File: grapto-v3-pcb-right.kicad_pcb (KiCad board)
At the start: 2 copper layers, 134.1 x 25.9 mm, 2 parts

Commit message: Switch positions.
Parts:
- added D10: D, Diode_SMD:D_SOD-323_HandSoldering, F.Cu at (114.3, 326.6)
- added D11: D, Diode_SMD:D_SOD-323_HandSoldering, F.Cu at (109.2, 329.5)
- added D12: D, Diode_SMD:D_SOD-323_HandSoldering, F.Cu at (119.3, 323.6)
- added D13: D, Diode_SMD:D_SOD-323_HandSoldering, F.Cu at (104.2, 329.5)
- added D14: D, Diode_SMD:D_SOD-323_HandSoldering, F.Cu at (99.2, 329.5)
- added D15: D, Diode_SMD:D_SOD-323_HandSoldering, F.Cu at (109.2, 326.6)
- added D16: D, Diode_SMD:D_SOD-323_HandSoldering, F.Cu at (84.0, 323.6)
- added D17: D, Diode_SMD:D_SOD-323_HandSoldering, F.Cu at (134.5, 323.6)
- added D18: D, Diode_SMD:D_SOD-323_HandSoldering, F.Cu at (89.0, 323.6)
- added D19: D, Diode_SMD:D_SOD-323_HandSoldering, F.Cu at (84.0, 326.6)
- added D20: D, Diode_SMD:D_SOD-323_HandSoldering, F.Cu at (89.0, 326.6)
- added D21: D, Diode_SMD:D_SOD-323_HandSoldering, F.Cu at (94.1, 323.6)
- added D22: D, Diode_SMD:D_SOD-323_HandSoldering, F.Cu at (99.2, 323.6)
- added D23: D, Diode_SMD:D_SOD-323_HandSoldering, F.Cu at (94.1, 326.6)
- added D24: D, Diode_SMD:D_SOD-323_HandSoldering, F.Cu at (89.0, 329.5)
- added D25: D, Diode_SMD:D_SOD-323_HandSoldering, F.Cu at (104.2, 323.6)
- added D26: D, Diode_SMD:D_SOD-323_HandSoldering, F.Cu at (94.1, 329.5)
- added D27: D, Diode_SMD:D_SOD-323_HandSoldering, F.Cu at (99.2, 326.6)
- added D28: D, Diode_SMD:D_SOD-323_HandSoldering, F.Cu at (104.2, 326.6)
- added D29: D, Diode_SMD:D_SOD-323_HandSoldering, F.Cu at (109.2, 323.6)
- added D3: D, Diode_SMD:D_SOD-323_HandSoldering, F.Cu at (119.3, 329.5)
- added D30: D, Diode_SMD:D_SOD-323_HandSoldering, F.Cu at (114.3, 323.6)
- added D4: D, Diode_SMD:D_SOD-323_HandSoldering, F.Cu at (114.3, 329.5)
- added D5: D, Diode_SMD:D_SOD-323_HandSoldering, F.Cu at (124.4, 326.6)
- added D6: D, Diode_SMD:D_SOD-323_HandSoldering, F.Cu at (129.4, 323.6)
- added D7: D, Diode_SMD:D_SOD-323_HandSoldering, F.Cu at (84.0, 329.5)
- added D8: D, Diode_SMD:D_SOD-323_HandSoldering, F.Cu at (124.4, 323.6)
- added D9: D, Diode_SMD:D_SOD-323_HandSoldering, F.Cu at (119.3, 326.6)
- added J1: USB_C_Receptacle, grapto-v3-pcb-right:Connector_GCT_USB4500, F.Cu at (234.4, 268.5)
- added J2: USB_C_Receptacle, grapto-v3-pcb-right:Connector_GCT_USB4500, F.Cu at (220.2, 268.5)
- added SW1: SW_Push, kaihl_choc:SW_Kailh_Choc_V1, F.Cu at (100.0, 43.0)
- added SW10: SW_Push, kaihl_choc:SW_Kailh_Choc_V1, F.Cu at (157.0, 56.0)
- added SW11: SW_Push, kaihl_choc:SW_Kailh_Choc_V1, F.Cu at (176.0, 75.0)
- added SW12: SW_Push, kaihl_choc:SW_Kailh_Choc_V1, F.Cu at (195.0, 94.0)
- added SW13: SW_Push, kaihl_choc:SW_Kailh_Choc_V1, F.Cu at (100.0, 81.0)
- added SW14: SW_Push, kaihl_choc:SW_Kailh_Choc_V1, F.Cu at (119.0, 75.0)
- added SW15: SW_Push, kaihl_choc:SW_Kailh_Choc_V1, F.Cu at (138.0, 70.0)
- added SW16: SW_Push, kaihl_choc:SW_Kailh_Choc_V1, F.Cu at (157.0, 75.0)
- added SW17: SW_Push, kaihl_choc:SW_Kailh_Choc_V1, F.Cu at (176.0, 94.0)
- added SW18: SW_Push, kaihl_choc:SW_Kailh_Choc_V1, F.Cu at (195.0, 113.0)
- added SW19: SW_Push, kaihl_choc:SW_Kailh_Choc_V1, F.Cu at (100.0, 100.0)
- added SW2: SW_Push, kaihl_choc:SW_Kailh_Choc_V1, F.Cu at (119.0, 37.0)
- added SW20: SW_Push, kaihl_choc:SW_Kailh_Choc_V1, F.Cu at (119.0, 94.0)
- added SW21: SW_Push, kaihl_choc:SW_Kailh_Choc_V1, F.Cu at (138.0, 89.0)
- added SW22: SW_Push, kaihl_choc:SW_Kailh_Choc_V1, F.Cu at (157.0, 94.0)
- added SW23: SW_Push, kaihl_choc:SW_Kailh_Choc_V1, F.Cu at (176.0, 113.0)
- added SW24: SW_Push, kaihl_choc:SW_Kailh_Choc_V1, F.Cu at (195.0, 147.0)
- added SW25: SW_Push, kaihl_choc:SW_Kailh_Choc_V1, F.Cu at (62.4, 143.7)
- added SW26: SW_Push, kaihl_choc:SW_Kailh_Choc_V1, F.Cu at (119.0, 113.0)
- added SW27: SW_Push, kaihl_choc:SW_Kailh_Choc_V1, F.Cu at (138.0, 108.0)
- added SW28: SW_Push, kaihl_choc:SW_Kailh_Choc_V1, F.Cu at (157.0, 113.0)
- added SW29: SW_Push, kaihl_choc:SW_Kailh_Choc_V1, F.Cu at (99.0, 120.8)
- added SW3: SW_Push, kaihl_choc:SW_Kailh_Choc_V1, F.Cu at (138.0, 32.0)
- added SW30: SW_Push, kaihl_choc:SW_Kailh_Choc_V1, F.Cu at (78.6, 128.9)
- added SW4: SW_Push, kaihl_choc:SW_Kailh_Choc_V1, F.Cu at (157.0, 37.0)
- added SW5: SW_Push, kaihl_choc:SW_Kailh_Choc_V1, F.Cu at (176.0, 56.0)
- added SW6: SW_Push, kaihl_choc:SW_Kailh_Choc_V1, F.Cu at (195.0, 75.0)
- added SW7: SW_Push, kaihl_choc:SW_Kailh_Choc_V1, F.Cu at (100.0, 62.0)
- added SW8: SW_Push, kaihl_choc:SW_Kailh_Choc_V1, F.Cu at (119.0, 56.0)
- added SW9: SW_Push, kaihl_choc:SW_Kailh_Choc_V1, F.Cu at (138.0, 51.0)
- D1, D2: value LED -> D; footprint LED_THT:LED_D3.0mm -> Diode_SMD:D_SOD-323_HandSoldering
- moved D1 223.2 mm to (124.4, 329.5)
- moved D2 220.6 mm to (129.4, 326.6)
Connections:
- D1 pad 2: Net-(D1-Pad2) -> col0
- D2 pad 2: Net-(D2-Pad2) -> col1
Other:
- board size 134.1 x 25.9 mm -> 147.1 x 190.9 mm

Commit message: updated sw pos
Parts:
- J1, J2: moved to B.Cu
- moved J2 221.6 mm to (63.9, 111.5)
- moved J1 220.3 mm to (79.7, 111.5)
- moved SW10 2.00 mm to (157.0, 58.0)
- moved SW11 2.00 mm to (176.0, 77.0)
- moved SW12 2.00 mm to (195.0, 96.0)
- moved SW14 2.00 mm to (119.0, 77.0)
- moved SW15 2.00 mm to (138.0, 72.0)
- moved SW16 2.00 mm to (157.0, 77.0)
- moved SW17 2.00 mm to (176.0, 96.0)
- moved SW18 2.00 mm to (195.0, 115.0)
- moved SW2 2.00 mm to (119.0, 39.0)
- moved SW20 2.00 mm to (119.0, 96.0)
- moved SW21 2.00 mm to (138.0, 91.0)
- moved SW22 2.00 mm to (157.0, 96.0)
- moved SW23 2.00 mm to (176.0, 115.0)
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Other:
- board size 147.1 x 190.9 mm -> 48.3 x 22.9 mm

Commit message: Edge cuts
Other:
- board size 48.3 x 22.9 mm -> 150.2 x 129.8 mm
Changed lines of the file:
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@@
     )
   )
-  (gr_line (start 176.145 131.77) (end 127.885 131.77) (layer Edge.Cuts) (width 0.05))
-  (gr_line (start 171.065 154.63) (end 176.145 131.77) (layer Edge.Cuts) (width 0.05))
-  (gr_line (start 132.965 154.63) (end 171.065 154.63) (layer Edge.Cuts) (width 0.05))
-  (gr_line (start 127.885 131.77) (end 132.965 154.63) (layer Edge.Cuts) (width 0.05))
+  (gr_line (start 88.430 113.140) (end 88.430 114.640) (angle 90) (layer Edge.Cuts) (width 0.05))
+  (gr_line (start 88.430 114.640) (end 94.630 114.640) (angle 90) (layer Edge.Cuts) (width 0.05))
+  (gr_arc (start 94.630 110.940) (end 94.630 114.640) (angle -180.000) (layer Edge.Cuts) (width 0.05))
+  (gr_line (start 94.630 107.240) (end 92.830 107.240) (angle 90) (layer Edge.Cuts) (width 0.05))
+  (gr_line (start 92.830 107.240) (end 92.830 35.037) (angle 90) (layer Edge.Cuts) (width 0.05))
+  (gr_arc (start 93.330 35.037) (end 93.225 34.549) (angle -77.903) (layer Edge.Cuts) (width 0.05))
+  (gr_line (start 93.225 34.549) (end 103.932 32.254) (angle 90) (layer Edge.Cuts) (width 0.05))
+  (gr_arc (start 104.037 32.743) (end 104.537 32.743) (angle -102.097) (layer Edge.Cuts) (width 0.05))
+  (gr_line (start 104.537 32.743) (end 104.537 32.763) (angle 90) (layer Edge.Cuts) (width 0.05))
+  (gr_arc (start 108.237 32.763) (end 104.537 32.763) (angle -180.000) (layer Edge.Cuts) (width 0.05))
+  (gr_line (start 112.332 30.454) (end 131.524 26.340) (angle 90) (layer Edge.Cuts) (width 0.05))
+  (gr_arc (start 131.629 26.829) (end 131.629 26.329) (angle -12.097) (layer Edge.Cuts) (width 0.05))
+  (gr_line (start 131.629 26.329) (end 144.276 26.329) (angle 90) (layer Edge.Cuts) (width 0.05))
+  (gr_arc (start 144.276 26.829) (end 144.403 26.346) (angle -14.737) (layer Edge.Cuts) (width 0.05))
+  (gr_line (start 144.403 26.346) (end 163.798 31.447) (angle 90) (layer Edge.Cuts) (width 0.05))
+  (gr_arc (start 163.671 31.931) (end 164.007 31.561) (angle -27.500) (layer Edge.Cuts) (width 0.05))
+  (gr_line (start 164.007 31.561) (end 192.921 57.813) (angle 90) (layer Edge.Cuts) (width 0.05))
+  (gr_line (start 202.178 67.427) (end 202.178 155.674) (angle 90) (layer Edge.Cuts) (width 0.05))
+  (gr_arc (start 201.678 155.674) (end 201.678 156.174) (angle -90.000) (layer Edge.Cuts) (width 0.05))
+  (gr_line (start 201.678 156.174) (end 186.978 156.174) (angle 90) (layer Edge.Cuts) (width 0.05))
+  (gr_line (start 63.846 153.805) (end 52.166 144.879) (angle 90) (layer Edge.Cuts) (width 0.05))
+  (gr_arc (start 52.470 144.482) (end 51.970 144.482) (angle -52.610) (layer Edge.Cuts) (width 0.05))
+  (gr_line (start 51.970 144.482) (end 51.970 113.140) (angle 90) (layer Edge.Cuts) (width 0.05))
+  (gr_line (start 51.970 113.140) (end 57.005 113.140) (angle 90) (layer Edge.Cuts) (width 0.05))
+  (gr_arc (start 112.437 30.942) (end 112.332 30.454) (angle -77.903) (layer Edge.Cuts) (width 0.05))
+  (gr_line (start 111.937 30.942) (end 111.937 32.763) (angle 90) (layer Edge.Cuts) (width 0.05))
+  (gr_arc (start 193.678 63.227) (end 190.939 60.740) (angle -132.237) (layer Edge.Cuts) (width 0.05))
+  (gr_arc (start 192.585 58.183) (end 192.956 58.519) (angle -90.000) (layer Edge.Cuts) (width 0.05))
+  (gr_line (start 192.956 58.519) (end 190.939 60.740) (angle 90) (layer Edge.Cuts) (width 0.05))
+  (gr_line (start 193.678 66.927) (end 201.678 66.927) (angle 90) (layer Edge.Cuts) (width 0.05))
+  (gr_arc (start 201.678 67.427) (end 202.178 67.427) (angle -90.000) (layer Edge.Cuts) (width 0.05))
+  (gr_arc (start 182.778 154.374) (end 186.478 154.374) (angle -180.000) (layer Edge.Cuts) (width 0.05))
+  (gr_line (start 186.478 154.374) (end 186.478 155.674) (angle 90) (layer Edge.Cuts) (width 0.05))
+  (gr_line (start 179.078 154.374) (end 179.078 155.674) (angle 90) (layer Edge.Cuts) (width 0.05))
+  (gr_line (start 178.578 156.174) (end 73.279 156.174) (angle 90) (layer Edge.Cuts) (width 0.05))
+  (gr_arc (start 186.978 155.674) (end 186.478 155.674) (angle -90.000) (layer Edge.Cuts) (width 0.05))
+  (gr_arc (start 178.578 155.674) (end 178.578 156.174) (angle -90.000) (layer Edge.Cuts) (width 0.05))
+  (gr_arc (start 69.079 153.874) (end 72.779 153.874) (angle -142.610) (layer Edge.Cuts) (width 0.05))
+  (gr_line (start 66.140 151.627) (end 64.547 153.712) (angle 90) (layer Edge.Cuts) (width 0.05))
+  (gr_line (start 72.779 153.874) (end 72.779 155.674) (angle 90) (layer Edge.Cuts) (width 0.05))
+  (gr_arc (start 64.149 153.408) (end 63.846 153.805) (angle -90.000) (layer Edge.Cuts) (width 0.05))
+  (gr_arc (start 73.279 155.674) (end 72.779 155.674) (angle -90.000) (layer Edge.Cuts) (width 0.05))
+  (gr_line (start 75.005 113.140) (end 75.005 119.340) (angle 90) (layer Edge.Cuts) (width 0.05))
+  (gr_line (start 75.005 119.340) (end 84.245 119.340) (angle 90) (layer Edge.Cuts) (width 0.05))
+  (gr_line (start 84.245 119.340) (end 84.245 113.140) (angle 90) (layer Edge.Cuts) (width 0.05))
+  (gr_line (start 66.245 113.140) (end 66.245 119.340) (angle 90) (layer Edge.Cuts) (width 0.05))
+  (gr_line (start 66.245 119.340) (end 57.005 119.340) (angle 90) (layer Edge.Cuts) (width 0.05))
+  (gr_line (start 57.005 119.340) (end 57.005 113.140) (angle 90) (layer Edge.Cuts) (width 0.05))
+  (gr_line (start 66.245 113.140) (end 75.005 113.140) (angle 90) (layer Edge.Cuts) (width 0.05))
+  (gr_line (start 84.245 113.140) (end 88.430 113.140) (angle 90) (layer Edge.Cuts) (width 0.05))
 )

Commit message: Fix usb connectors
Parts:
- J1, J2: value USB_C_Receptacle -> USB_C_Receptacle_USB2.0
- moved J1 18.2 mm to (61.6, 113.1)
- moved J2 15.8 mm to (79.6, 113.1)

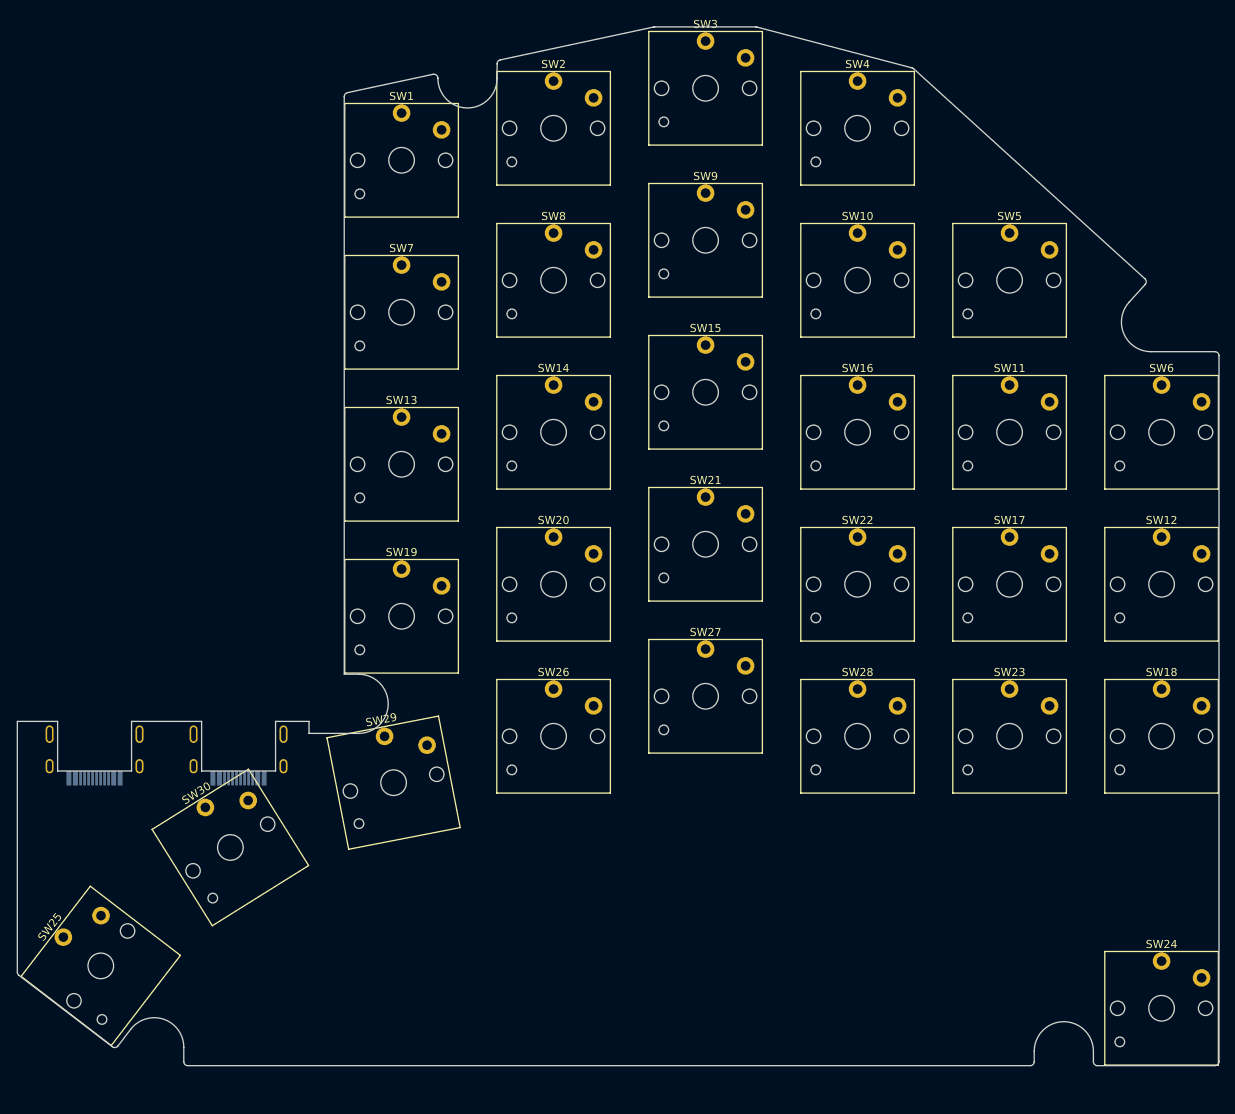
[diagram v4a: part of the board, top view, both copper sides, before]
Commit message: Update thumb positions
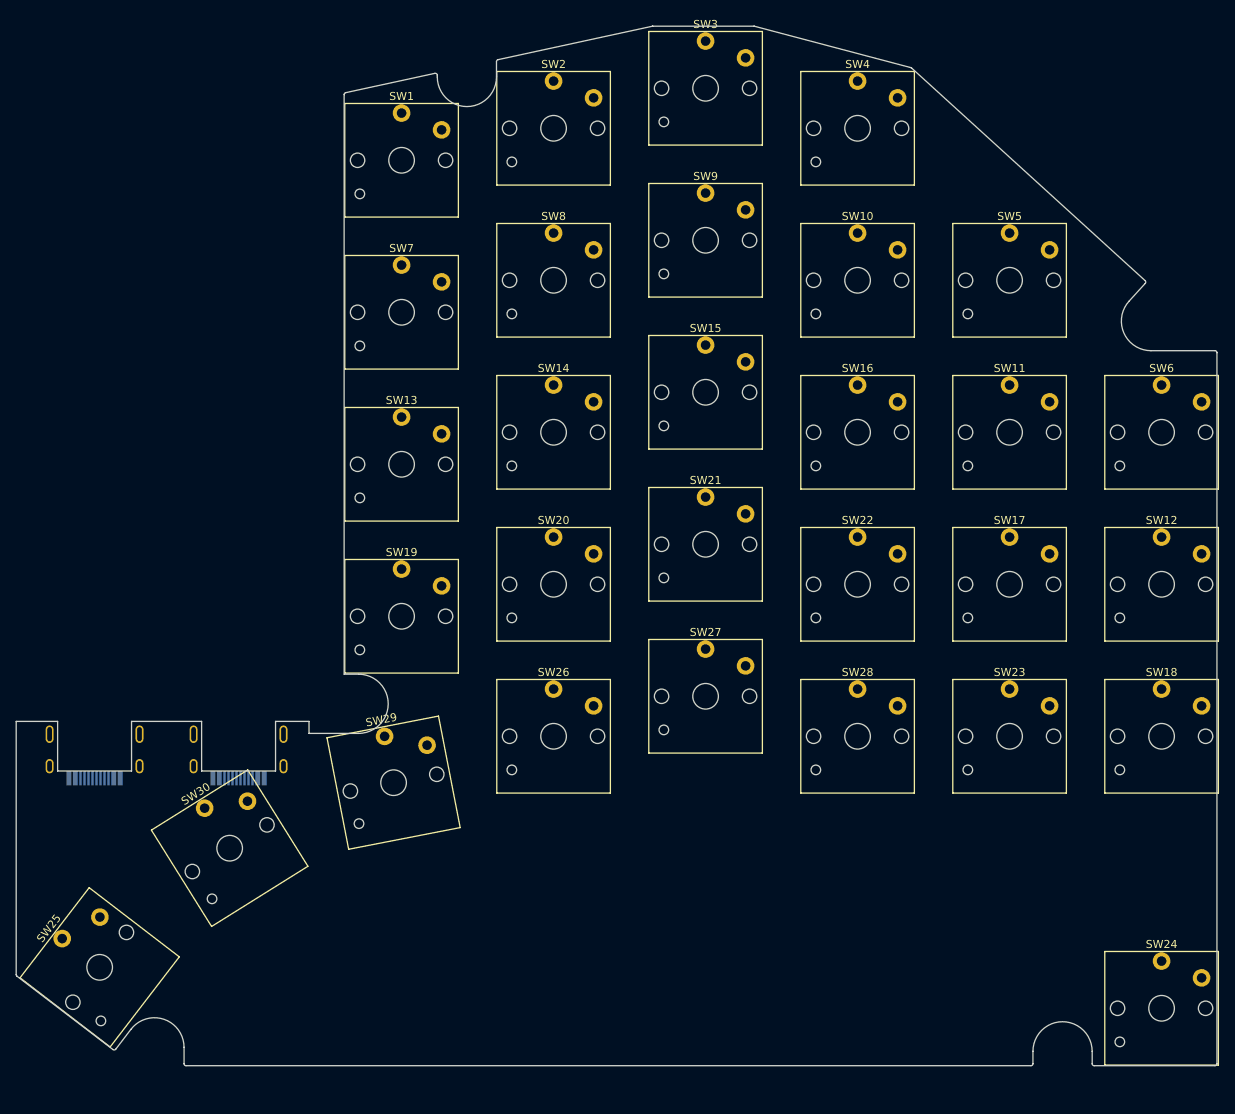
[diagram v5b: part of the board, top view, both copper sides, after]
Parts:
- moved SW25 0.23 mm to (62.3, 143.9)
- moved SW30 0.13 mm to (78.5, 129.0)
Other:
- board size 150.2 x 129.8 mm -> 150.1 x 129.9 mm

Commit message: udpate
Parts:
- J1, J2: footprint grapto-v3-pcb-right:Connector_GCT_USB4500 -> grapto-v3-schematic:Connector_GCT_USB4500

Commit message: Initial routing
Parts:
- added C1: .1u, Capacitor_SMD:C_0603_1608Metric_Pad1.08x0.95mm_HandSolder, B.Cu at (92.5, 145.3)
- added C10: 32p, Capacitor_SMD:C_0805_2012Metric_Pad1.18x1.45mm_HandSolder, B.Cu at (107.7, 131.5)
- added C11: 32p, Capacitor_SMD:C_0805_2012Metric_Pad1.18x1.45mm_HandSolder, B.Cu at (104.7, 127.2)
- added C12: 1u, Capacitor_SMD:C_0603_1608Metric_Pad1.08x0.95mm_HandSolder, B.Cu at (95.8, 132.5)
- added C2: .1u, Capacitor_SMD:C_0603_1608Metric_Pad1.08x0.95mm_HandSolder, B.Cu at (92.5, 140.4)
- added C3: .1u, Capacitor_SMD:C_0603_1608Metric_Pad1.08x0.95mm_HandSolder, B.Cu at (98.8, 131.7)
- added C4: .1u, Capacitor_SMD:C_0603_1608Metric_Pad1.08x0.95mm_HandSolder, B.Cu at (113.6, 138.5)
- added C5: .1u, Capacitor_SMD:C_0603_1608Metric_Pad1.08x0.95mm_HandSolder, B.Cu at (110.0, 149.2)
- added C6: .1u, Capacitor_SMD:C_0603_1608Metric_Pad1.08x0.95mm_HandSolder, B.Cu at (96.9, 150.2)
- added C7: 1u, Capacitor_SMD:C_0603_1608Metric_Pad1.08x0.95mm_HandSolder, B.Cu at (113.6, 145.7)
- added C8: .1u, Capacitor_SMD:C_0603_1608Metric_Pad1.08x0.95mm_HandSolder, B.Cu at (99.7, 151.7)
- added C9: 1u, Capacitor_SMD:C_0603_1608Metric_Pad1.08x0.95mm_HandSolder, B.Cu at (92.5, 142.0)
- added D31: LED, Diode_SMD:D_0805_2012Metric_Pad1.15x1.40mm_HandSolder, B.Cu at (91.1, 148.3)
- added F1: 200m, Fuse:Fuse_0603_1608Metric_Pad1.05x0.95mm_HandSolder, B.Cu at (92.3, 132.6)
- added R1: 22, Resistor_SMD:R_0603_1608Metric_Pad0.98x0.95mm_HandSolder, B.Cu at (86.7, 131.5)
- added R4: 4.7k, Resistor_SMD:R_0603_1608Metric_Pad0.98x0.95mm_HandSolder, B.Cu at (112.7, 135.9)
- added R5: 5.1k, Resistor_SMD:R_0603_1608Metric_Pad0.98x0.95mm_HandSolder, B.Cu at (83.7, 131.5)
- added R6: 5.1k, Resistor_SMD:R_0603_1608Metric_Pad0.98x0.95mm_HandSolder, B.Cu at (88.2, 131.5)
- added R7: 22, Resistor_SMD:R_0603_1608Metric_Pad0.98x0.95mm_HandSolder, B.Cu at (85.2, 131.5)
- added R8: 68, Resistor_SMD:R_0603_1608Metric_Pad0.98x0.95mm_HandSolder, B.Cu at (87.4, 148.3)
- added SW31: SW_SPST, grapto-v3-schematic:Switch_TL3315NF100Q, B.Cu at (116.9, 131.3)
- added TP1: TestPoint, grapto-v3-schematic:TestPoint_S2761-46R, B.Cu at (92.3, 136.0)
- added U1: ATmega32U4-AU, grapto-v3-schematic:QFP-44_10x10_Pitch0.8mm_Hand_solder, B.Cu at (102.9, 141.7)
- added Y1: Crystal_GND24, grapto-v3-schematic:Crystal_ECS-160-20-33-TR3, B.Cu at (103.2, 130.4)
- D1, D10, D11, D12, D13, D14, D15, D16, D17, D18, D19, D2, D20, D21, D22, D23, D24, D25, D26, D27, D28, D29, D3, D30, D4, D5, D6, D7, D8, D9: footprint Diode_SMD:D_SOD-323_HandSoldering -> Diode_SMD:D_SOD-123; moved to B.Cu
- moved D3 292.6 mm to (142.7, 37.8)
- moved D4 290.9 mm to (161.5, 42.5)
- moved D2 284.1 mm to (123.8, 42.5)
- moved D1 276.9 mm to (95.0, 54.2), turned to 270 degrees
- moved D9 271.0 mm to (142.5, 56.5)
- moved D10 269.1 mm to (161.4, 61.6)
- moved D5 263.3 mm to (172.6, 67.7), turned to 270 degrees
- moved D8 262.3 mm to (123.5, 61.3)
- moved D7 255.9 mm to (95.0, 73.8), turned to 270 degrees
- moved D16 255.1 mm to (161.3, 80.5)
- moved D15 253.1 mm to (142.5, 75.6)
- moved D11 252.0 mm to (173.1, 85.7), turned to 270 degrees
- moved D14 250.2 mm to (124.0, 80.5)
- moved D6 246.3 mm to (188.5, 84.5), turned to 180 degrees
- moved D13 239.6 mm to (95.2, 90.1), turned to 270 degrees
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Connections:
- net col0 renamed /Sheet6188018D/col0
- net col1 renamed /Sheet6188018D/col1
- net col2 renamed /Sheet6188018D/col2
- net col3 renamed /Sheet6188018D/col3
- net col4 renamed /Sheet6188018D/col4
- net col5 renamed /Sheet6188018D/col5
- net row0 renamed /Sheet6188018D/row0
- net row1 renamed /Sheet6188018D/row1
- net row2 renamed /Sheet6188018D/row2
- net row3 renamed /Sheet6188018D/row3
- net row4 renamed /Sheet6188018D/row4
- J1 pad A12: Net-(J1-PadA1) -> 0V
- J1 pad A4: Net-(J1-PadA4) -> VBUS
- J1 pad A6: Net-(J1-PadA6) -> /Sheet61884E9A/SCL
- J1 pad A7: Net-(J1-PadA7) -> /Sheet61884E9A/SDA
- J1 pad B12: Net-(J1-PadA1) -> 0V
- J1 pad B4: Net-(J1-PadA4) -> VBUS
- J1 pad B6: Net-(J1-PadB6) -> /Sheet61884E9A/SCL
- J1 pad B7: Net-(J1-PadB7) -> /Sheet61884E9A/SDA
- J1 pad S1: Net-(J1-PadS1) -> 0V
- J2 pad A12: Net-(J2-PadA1) -> 0V
- J2 pad A4: Net-(J2-PadA4) -> VBUS
- J2 pad A6: Net-(J2-PadA6) -> /Sheet61884E9A/USB_FULL_P1
- J2 pad A7: Net-(J2-PadA7) -> /Sheet61884E9A/USB_FULL_N1
- J2 pad B12: Net-(J2-PadA1) -> 0V
- J2 pad B4: Net-(J2-PadA4) -> VBUS
- J2 pad B6: Net-(J2-PadB6) -> /Sheet61884E9A/USB_FULL_P1
- J2 pad B7: Net-(J2-PadB7) -> /Sheet61884E9A/USB_FULL_N1
- J2 pad S1: Net-(J2-PadS1) -> 0V
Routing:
- net /Sheet6188018D/row3: track 0.00 -> 133.9 mm
- net /Sheet6188018D/row2: track 0.00 -> 124.4 mm
- net /Sheet6188018D/row1: track 0.00 -> 123.5 mm
- net /Sheet6188018D/row0: track 0.00 -> 123.3 mm
- net /Sheet6188018D/row4: track 0.00 -> 101.4 mm, vias 0 -> 2
- net 5V: track 0.00 -> 100.9 mm
- net /Sheet61884E9A/SDA: track 0.00 -> 76.8 mm, vias 0 -> 4
- net VBUS: track 0.00 -> 76.5 mm, vias 0 -> 2
- net /Sheet61884E9A/SCL: track 0.00 -> 73.9 mm, vias 0 -> 2
- net /Sheet61884E9A/~RST: track 0.00 -> 34.8 mm
- net /Sheet61884E9A/USB_FULL_N1: track 0.00 -> 21.5 mm
- net /Sheet61884E9A/USB_FULL_P1: track 0.00 -> 21.3 mm, vias 0 -> 2
- net /Sheet61884E9A/USB_FULL_N: track 0.00 -> 19.3 mm
- net /Sheet61884E9A/USB_FULL_P: track 0.00 -> 19.0 mm
- net /Sheet6188018D/col5: track 0.00 -> 14.5 mm, vias 0 -> 2
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- added copper zone on F.Cu, net 0V
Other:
- net class Default: trace_width 0.25 -> 0.15
- net class PWR added: clearance 0.2, trace_width 0.4, via_dia 0.8, via_drill 0.4
- rule trace_min: 0.2 -> 0.15
